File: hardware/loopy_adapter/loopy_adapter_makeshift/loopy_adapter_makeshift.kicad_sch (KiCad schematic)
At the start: 8 parts, among them J1 CART SLOT TOP ROW, J2 CART SLOT BOTTOM ROW, J3 Conn_02x06_Counter_Clockwise, J4 Conn_02x06_Counter_Clockwise, J5 Loopy_Cart_Side, J6 Loopy_Cart_Side, J7 Conn_02x06_Counter_Clockwise, J8 Conn_02x06_Counter_Clockwise

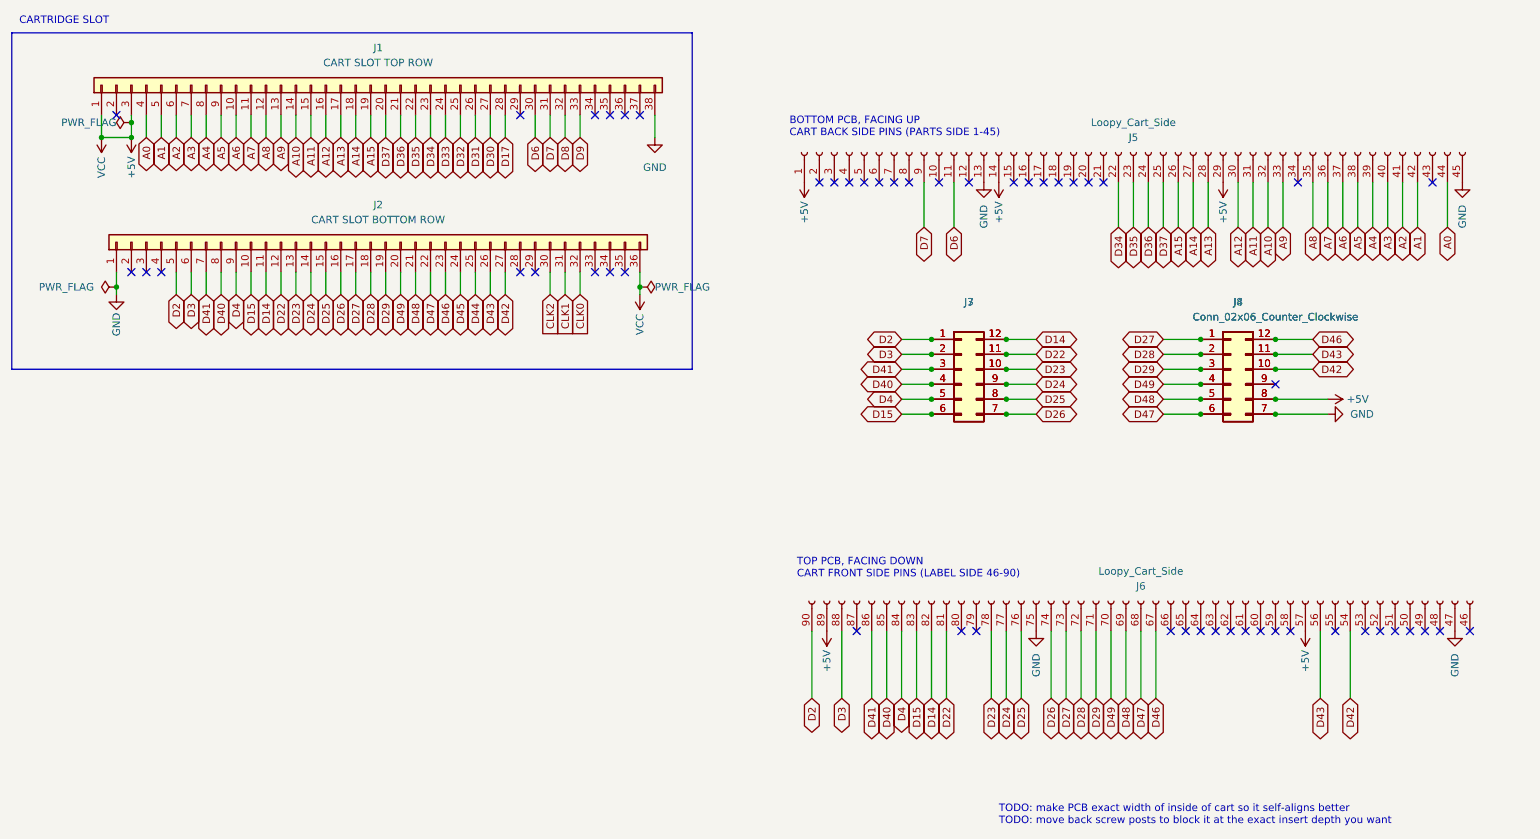
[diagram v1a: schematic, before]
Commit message: Tweaking schematic to better identify shorts
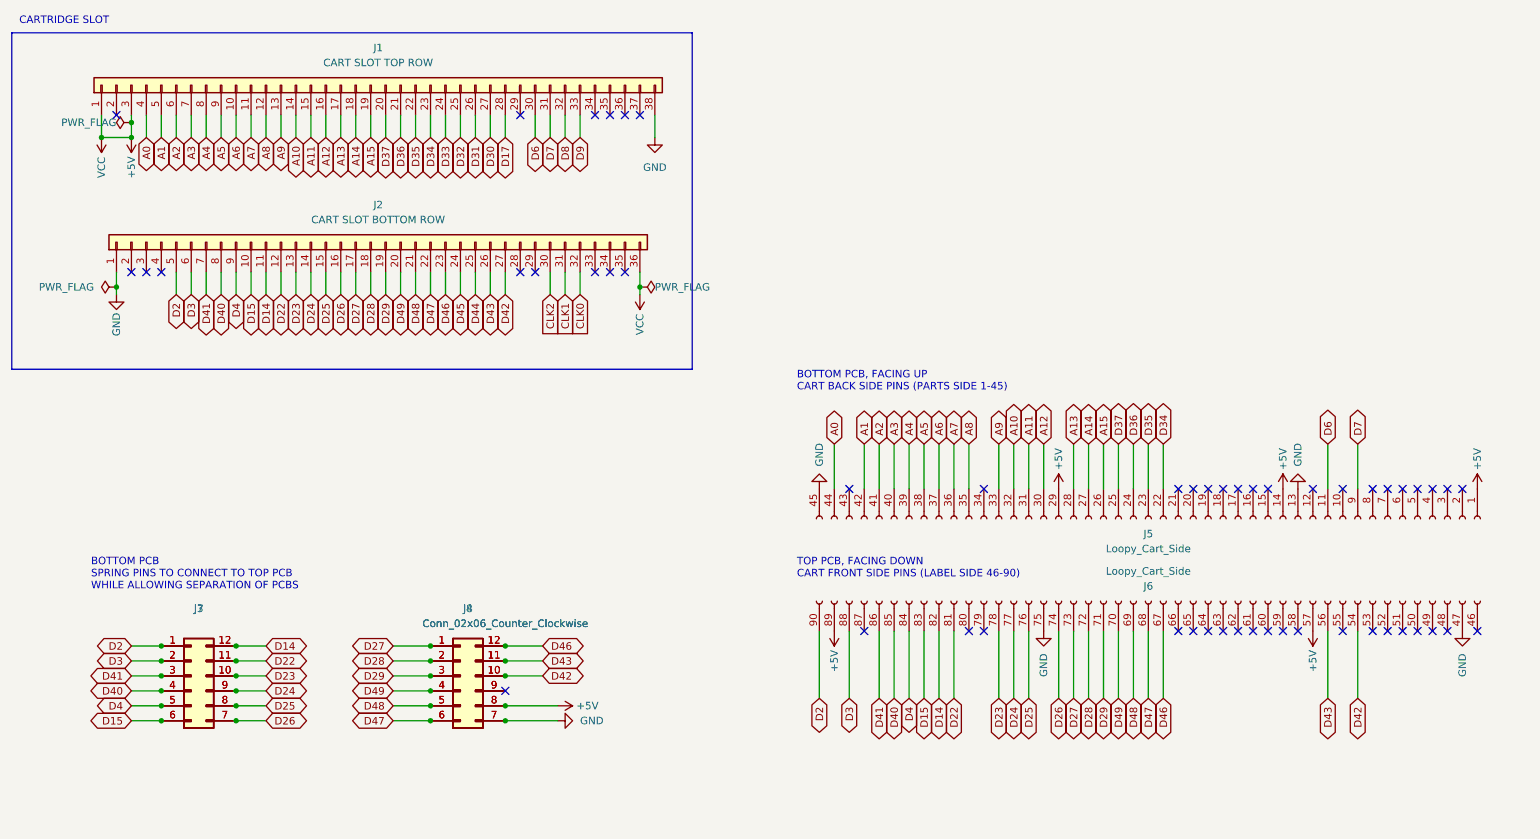
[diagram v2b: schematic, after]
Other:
- note added: "BOTTOM PCB SPRING PINS TO CONNECT TO TOP PCB WHILE ALLOWING SEPARATION OF PCBS"
- note removed: "TODO: make PCB exact width of inside of cart so it self-aligns better TODO: move back screw posts to block it at the exact insert depth you want"
- moved on the sheet: J3, J4, J5, J6, J7, J8
